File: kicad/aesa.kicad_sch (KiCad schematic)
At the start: 0 parts

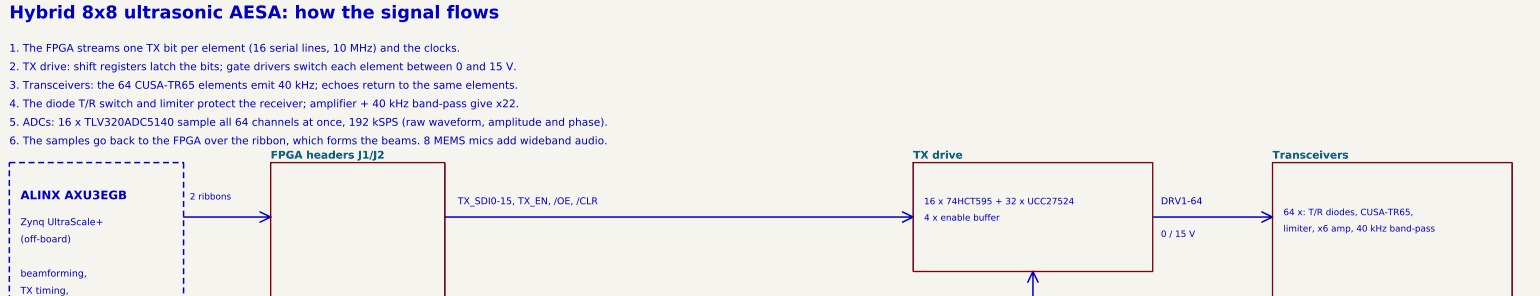
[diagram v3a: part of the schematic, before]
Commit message: Transducer: Same Sky CUSP-TR80-15-2500-TH instead of CUSA-TR65 (about $122 less per board)
- Ø9.8 mm 40 kHz transceiver, 105 dB SPL, 0.2-15 m, 1.6 ms ring-down, 2.0 nF; $1.65 (Future,
  DigiKey second source); not sealed (indoor, behind the waveguide)
- new footprint aesa:CUSP-TR80 (5.0 mm pin pitch, Ø2 mm pads, Ø0.9 mm holes, '+' = pad 1);
  CUSA-TR65 footprint removed; soldering keep-out follows the larger pads
- simulation model CUSP_TR80 (C0 2.0 nF; Rm 3 k and the 1 m echo level kept as assumptions):
  all 10 simulations pass
- BOM total $326 per board (was $444); datasheet library, checks, brief and README updated;
  board re-placed, DRC 0 violations
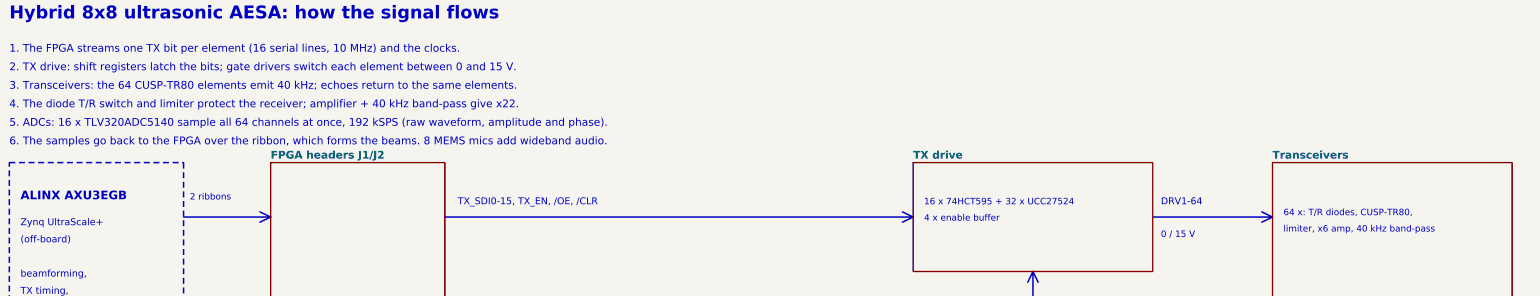
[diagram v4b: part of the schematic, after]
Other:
- note added: "3. Transceivers: the 64 CUSP-TR80 elements emit 40 kHz; echoes return to the same elements."
- note added: "64 x: T/R diodes, CUSP-TR80,"
- note removed: "3. Transceivers: the 64 CUSA-TR65 elements emit 40 kHz; echoes return to the same elements."
- note removed: "64 x: T/R diodes, CUSA-TR65,"
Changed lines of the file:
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@@
 		)
 	)
-	(text "3. Transceivers: the 64 CUSA-TR65 elements emit 40 kHz; echoes return to the same elements."
+	(text "3. Transceivers: the 64 CUSP-TR80 elements emit 40 kHz; echoes return to the same elements."
 		(exclude_from_sim no)
 		(at 25.40 44.20 0)
@@
 		)
 	)
-	(text "64 x: T/R diodes, CUSA-TR65,"
+	(text "64 x: T/R diodes, CUSP-TR80,"
 		(exclude_from_sim no)
 		(at 322.58 73.66 0)

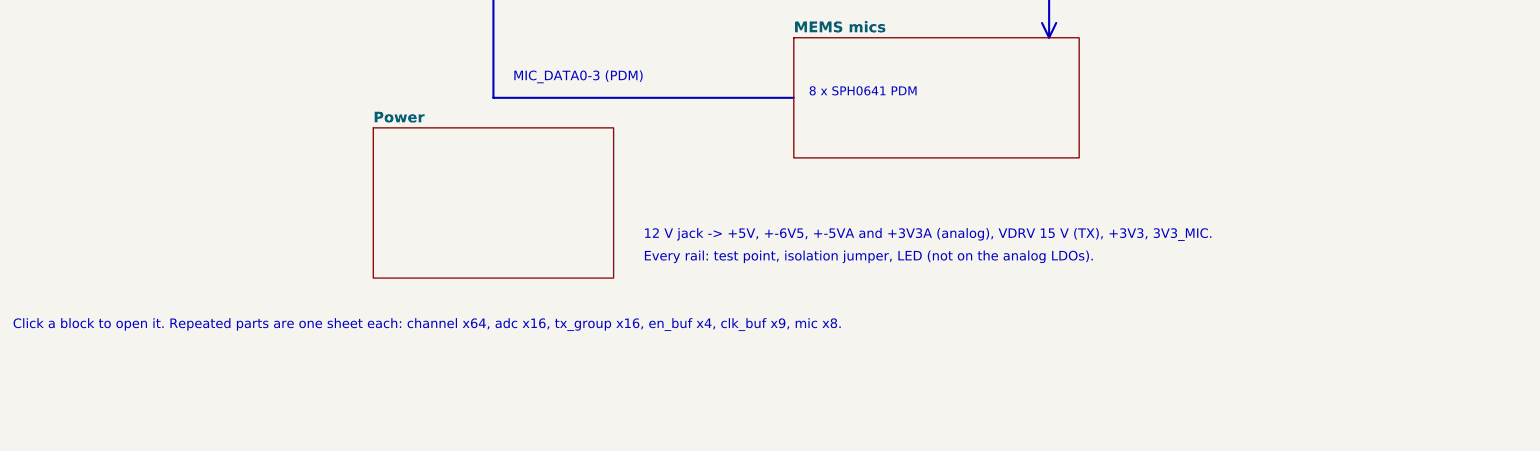
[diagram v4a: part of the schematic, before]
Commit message: Board ready for routing: power sheets redrawn, 3D models, test access, routing setup
Schematic
- Power supply split into two boxed A3 sheets (Power 1: input, +5V, VDRV,
  +3V3, 3V3_MIC; Power 2: analog +-6V5, +-5VA, +3V3A and the bring-up notes);
  eFuse wired inline; text no longer clashes; ferrite drawn as L_Ferrite.
- Every page of the schematic PDF is A3 (cells scaled up, array redrawn).
- RX_OUT test pad on every channel; four more GND test points.
- Test pads and solder jumpers out of the BOM, like their footprints.

Board
- 3D model for every part (make_3d.py for the CUSP-TR80, stock substitutes
  for four missing library models); check_design checks it.
- JLC04161H-7628 stackup, ENIG; inner GND layers typed as planes; thermal
  reliefs on through-hole pads; HighCurrent net class (1 mm).
- Custom DRC rules (aesa.kicad_dru): TX/RX and switch-node separation,
  clock spacing, JLCPCB limits.
- Footprints keep their library IDs (schematic parity clean); assembly
  drawing docs/assembly/aesa_assembly.pdf.
- Freerouting 2.5.0 installed; DSN export checked.

ERC 0, DRC 0, design check 19/19, placement checks 12/12.
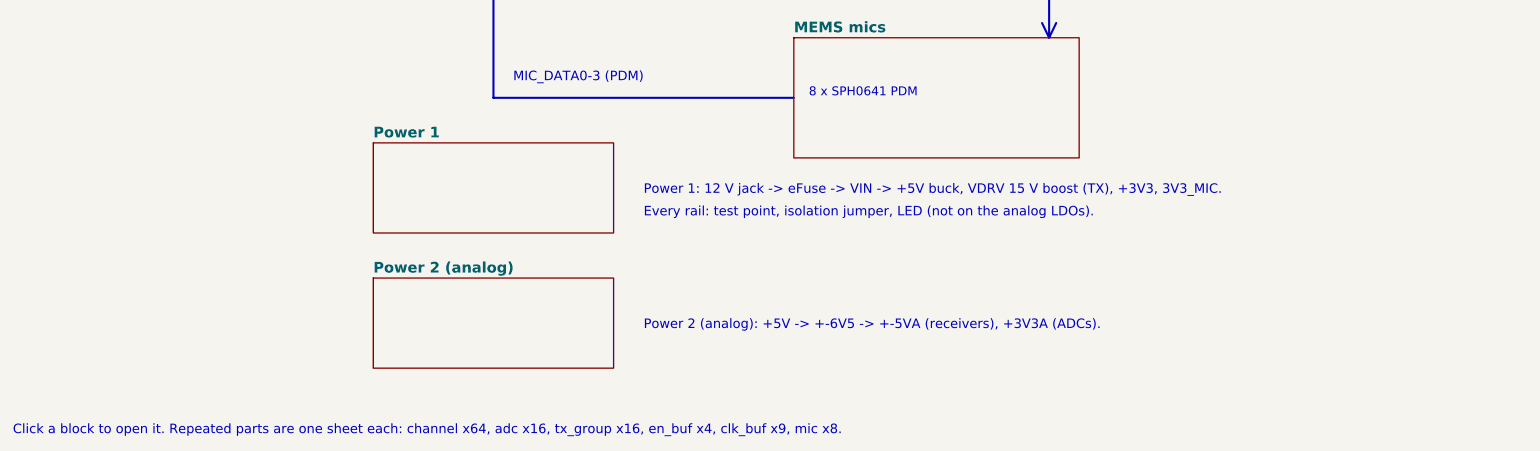
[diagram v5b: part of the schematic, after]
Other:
- removed sheet Power
- added sheet Power 1 (power.kicad_sch)
- added sheet Power 2 (analog) (power_analog.kicad_sch)
- note added: "Power 1: 12 V jack -> eFuse -> VIN -> +5V buck, VDRV 15 V boost (TX), +3V3, 3V3_MIC."
- note added: "Power 2 (analog): +5V -> +-6V5 -> +-5VA (receivers), +3V3A (ADCs)."
- note removed: "12 V jack -> +5V, +-6V5, +-5VA and +3V3A (analog), VDRV 15 V (TX), +3V3, 3V3_MIC."
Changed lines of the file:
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@@
 		)
 	)
-	(text "12 V jack -> +5V, +-6V5, +-5VA and +3V3A (analog), VDRV 15 V (TX), +3V3, 3V3_MIC."
+	(text "Power 1: 12 V jack -> eFuse -> VIN -> +5V buck, VDRV 15 V boost (TX), +3V3, 3V3_MIC."
 		(exclude_from_sim no)
-		(at 132.08 240.03 0)
+		(at 132.08 232.41 0)
 		(effects
 			(font
@@
 		)
 	)
-	(text "Every rail: test point, isolation jumper, LED (not on the analog LDOs)."
+	(text "Power 2 (analog): +5V -> +-6V5 -> +-5VA (receivers), +3V3A (ADCs)."
 		(exclude_from_sim no)
-		(at 132.08 243.84 0)
+		(at 132.08 255.27 0)
 		(effects
 			(font
@@
 		)
 	)
-	(text "Click a block to open it. Repeated parts are one sheet each: channel x64, adc x16, tx_group x16, en_buf x4, clk_buf x9, mic x8."
+	(text "Every rail: test point, isolation jumper, LED (not on the analog LDOs)."
 		(exclude_from_sim no)
-		(at 25.40 255.27 0)
+		(at 132.08 236.22 0)
 		(effects
 			(font
@@
 		)
 	)
+	(text "Click a block to open it. Repeated parts are one sheet each: channel x64, adc x16, tx_group x16, en_buf x4, clk_buf x9, mic x8."
+		(exclude_from_sim no)
+		(at 25.40 273.05 0)
+		(effects
+			(font
+				(size 1.6 1.6)
+			)
+			(justify left bottom)
+		)
+	)
 	(sheet
 		(at 86.36 60.96)
@@
 	)
 	(sheet
-		(at 86.36 220.98)
-		(size 40.64 25.40)
-		(fields_autoplaced yes)
-		(stroke
-			(width 0.1524)
-			(type solid)
-		)
-		(fill
-			(color 238 238 238 1.0000)
-		)
-		(property "Sheetname" "Power"
-			(at 86.36 220.27 0)
+		(at 86.36 223.52)
+		(size 40.64 15.24)
+		(fields_autoplaced yes)
+		(stroke
+			(width 0.1524)
+			(type solid)
+		)
+		(fill
+			(color 238 238 238 1.0000)
+		)
+		(property "Sheetname" "Power 1"
+			(at 86.36 222.81 0)
 			(effects
 				(font
@@
 		)
 		(property "Sheetfile" "power.kicad_sch"
-			(at 86.36 246.97 0)
+			(at 86.36 239.35 0)
 			(effects
 				(font
@@
 				)
 			)
+		)
+	)
+	(sheet
+		(at 86.36 246.38)
+		(size 40.64 15.24)
+		(fields_autoplaced yes)
+		(stroke
+			(width 0.1524)
+			(type solid)
+		)
+		(fill
+			(color 238 238 238 1.0000)
+		)
+		(property "Sheetname" "Power 2 (analog)"
+			(at 86.36 245.67 0)
+			(effects
+				(font
+					(size 1.8 1.8)
+					(bold yes)
+				)
+				(justify left bottom)
+			)
+		)
+		(property "Sheetfile" "power_analog.kicad_sch"
+			(at 86.36 262.21 0)
+			(effects
+				(font
+					(size 1.27 1.27)
+				)
+				(justify left top)
+				(hide yes)
+			)
+		)
+		(instances
+			(project "aesa"
+				(path "/35d88121-1d5f-4a62-9009-788ea6bf93dd"
+					(page "126")
+				)
+			)

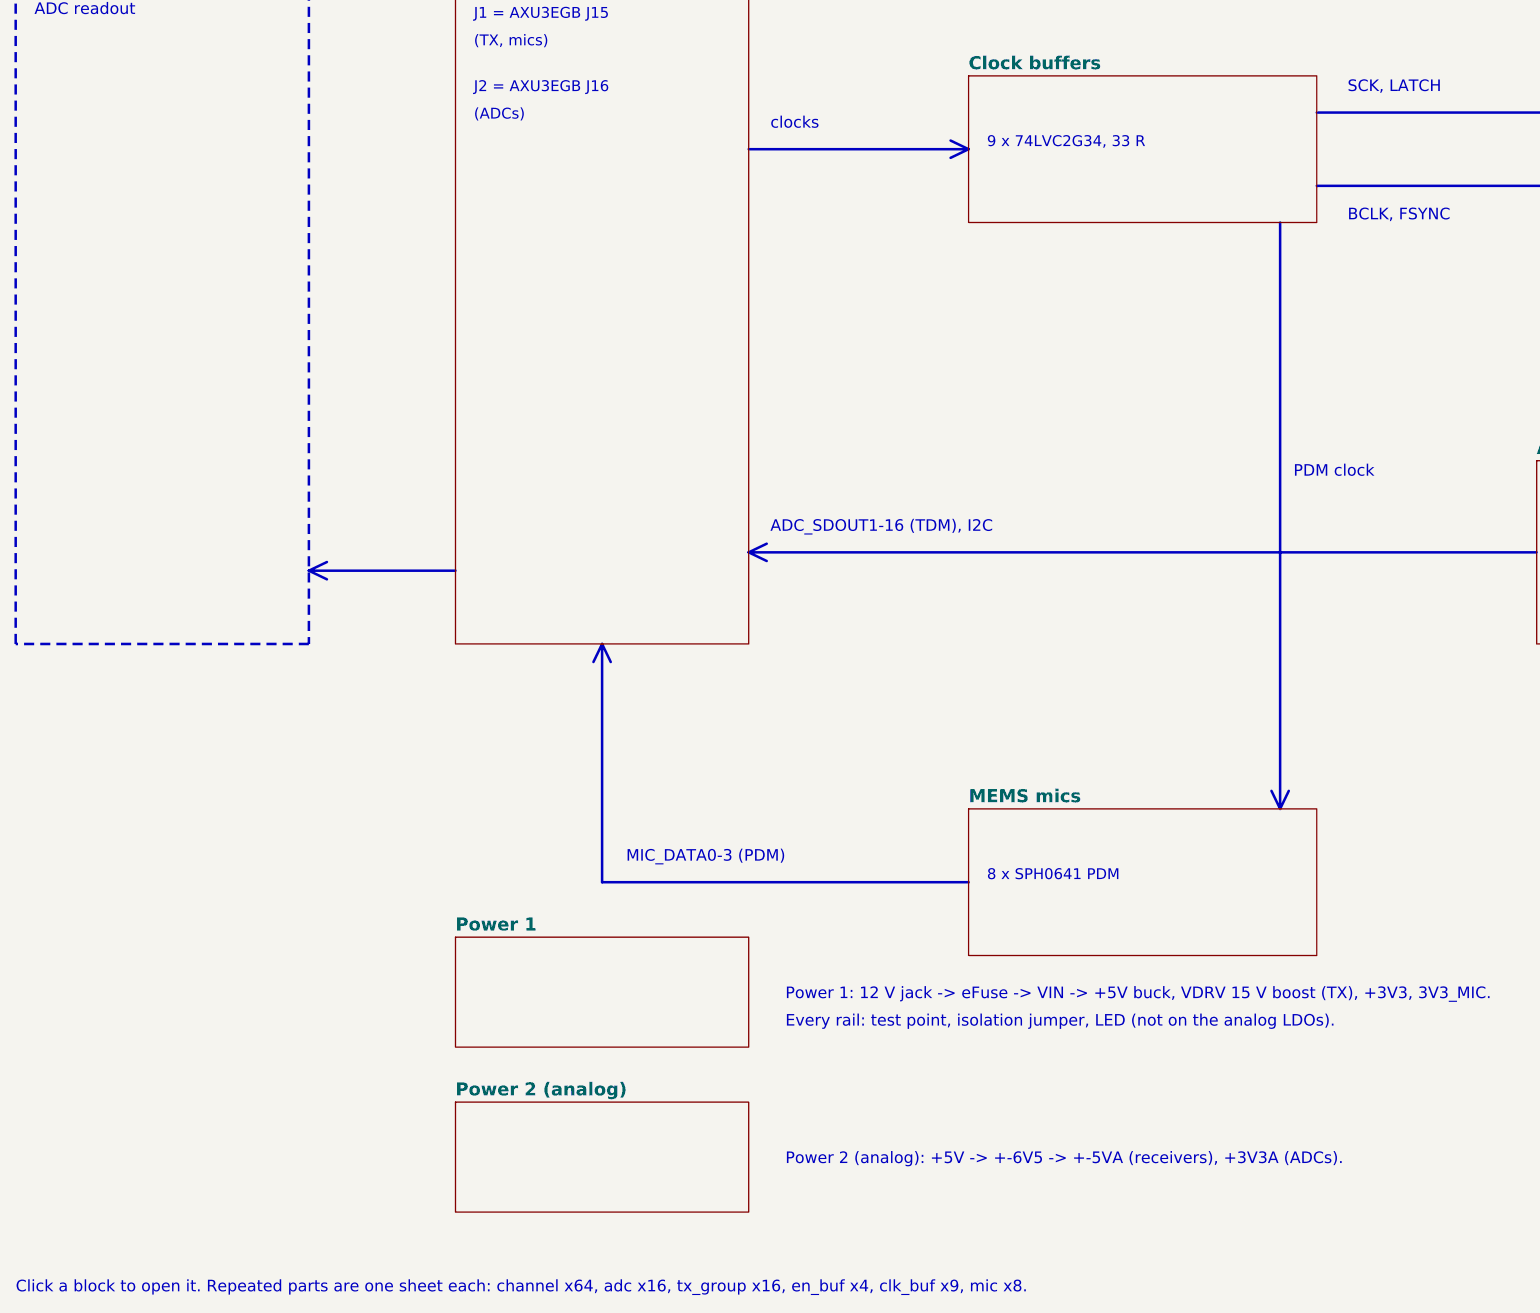
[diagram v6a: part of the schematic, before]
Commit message: Block-first routing: all repeated blocks routed and passing, power input and +-6V5 hand-routed
Schematic
- TX groups and ADC inputs numbered in order (TXG01 = DRV1-4, ADC IN1..4 = RX1..4).
- Power sheets renumbered 1-8 with real references; eFuse RTN no longer tied to GND (TPS2660 9.3.5.5).
- Damped 100 uF bulk caps at the far ends of VIN (C50) and +5V (C51); header clock RC filters removed;
  switch-node snubbers kept as DNP footprints.

Layout and routing
- New routing toolchain: route.py (block stages), block_routes.py (hand-made block routes), maze.py
  (45-degree grid router with rip-up and a per-net time budget), route_lib.py (bend45, chamfer, copper
  checks), block_check.py (DRC and internal nets per block instance), board/cell views.
- Channel, ADC, TX group, clock buffer, enable buffer, mic and header blocks routed and passing
  block_check; no right-angle corners left.
- Designed TX control bus; SDI taps keep 0.7 mm from clock copper.
- Power: 12 V input (eFuse, RTN island, FLT via the front copper) and TPS65131 +-6V5 section with fixed
  templates and hand routing; each power section counts as its own block; the +3V3 LED overflows into
  the gap beside its section.

docs/routing_and_emi.md describes the routing and EMI rules; sim/mic_clock_si adds the mic clock check.
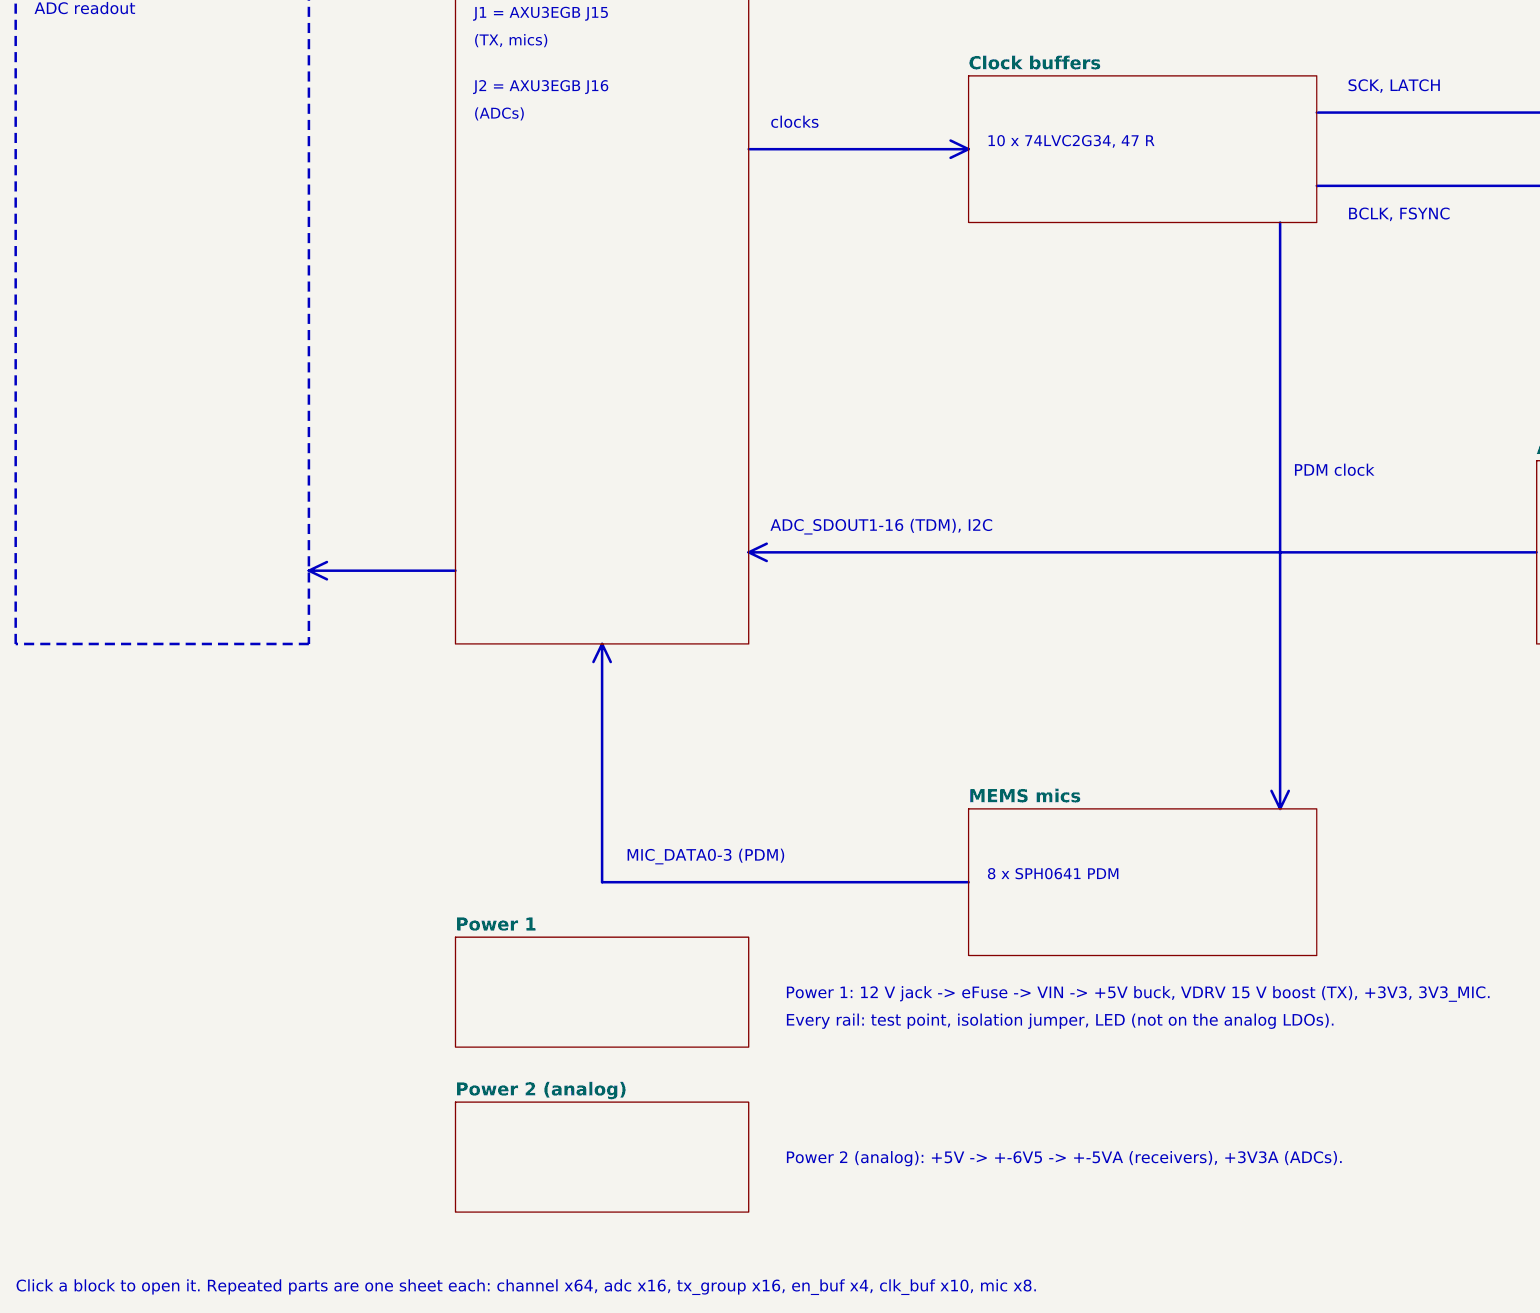
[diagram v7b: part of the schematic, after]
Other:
- note added: "10 x 74LVC2G34, 47 R"
- note added: "Click a block to open it. Repeated parts are one sheet each: channel x64, adc x16, tx_group x16, en_buf x4, clk_buf x10, mic x8."
- note removed: "9 x 74LVC2G34, 33 R"
- note removed: "Click a block to open it. Repeated parts are one sheet each: channel x64, adc x16, tx_group x16, en_buf x4, clk_buf x9, mic x8."
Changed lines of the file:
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@@
 		)
 	)
-	(text "9 x 74LVC2G34, 33 R"
+	(text "10 x 74LVC2G34, 47 R"
 		(exclude_from_sim no)
 		(at 160.02 114.30 0)
@@
 		)
 	)
-	(text "Click a block to open it. Repeated parts are one sheet each: channel x64, adc x16, tx_group x16, en_buf x4, clk_buf x9, mic x8."
+	(text "Click a block to open it. Repeated parts are one sheet each: channel x64, adc x16, tx_group x16, en_buf x4, clk_buf x10, mic x8."
 		(exclude_from_sim no)
 		(at 25.40 273.05 0)
@@
 			(project "aesa"
 				(path "/35d88121-1d5f-4a62-9009-788ea6bf93dd"
-					(page "13")
+					(page "14")
 				)
 			)
@@
 			(project "aesa"
 				(path "/35d88121-1d5f-4a62-9009-788ea6bf93dd"
-					(page "34")
+					(page "35")
 				)
 			)
@@
 			(project "aesa"
 				(path "/35d88121-1d5f-4a62-9009-788ea6bf93dd"
-					(page "99")
+					(page "100")
 				)
 			)
@@
 			(project "aesa"
 				(path "/35d88121-1d5f-4a62-9009-788ea6bf93dd"
-					(page "116")
+					(page "117")
 				)
 			)
@@
 			(project "aesa"
 				(path "/35d88121-1d5f-4a62-9009-788ea6bf93dd"
-					(page "125")
+					(page "126")
 				)
 			)
@@
 			(project "aesa"
 				(path "/35d88121-1d5f-4a62-9009-788ea6bf93dd"
-					(page "126")
-				)
-			)
+					(page "127")
+				)
+			)
